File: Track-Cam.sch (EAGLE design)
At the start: 40 parts, among them IC1 STM32F042K6T, IC2 BD6211F, IC3 BD6211F, Q1 8MHz, X1 RASPI_BOARD_B+#_HC

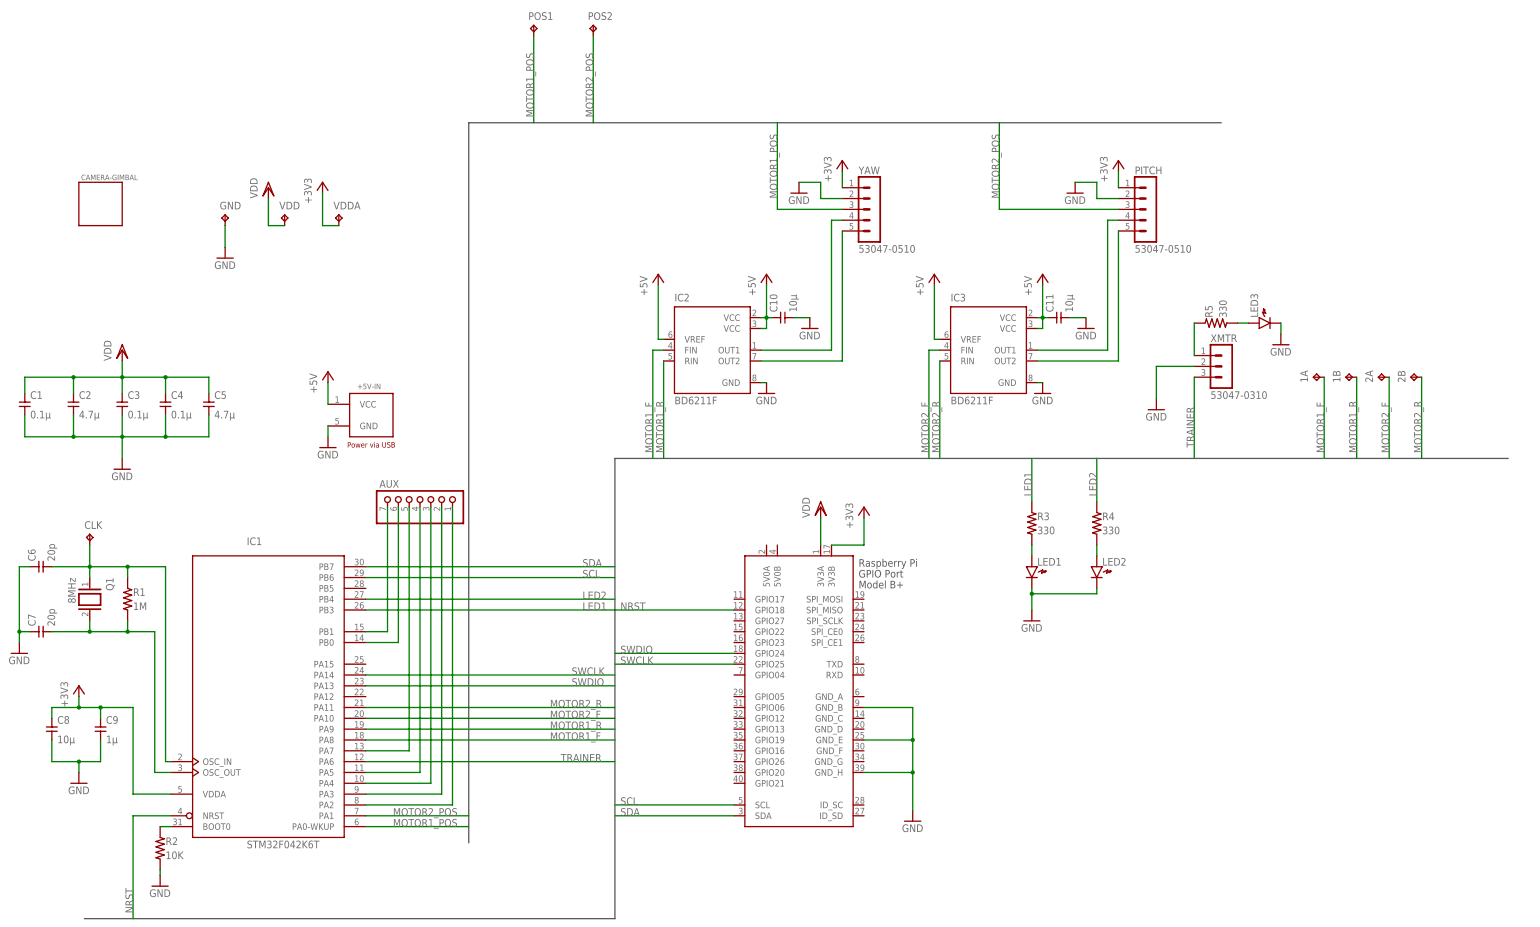
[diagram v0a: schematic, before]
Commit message: enlarge pads
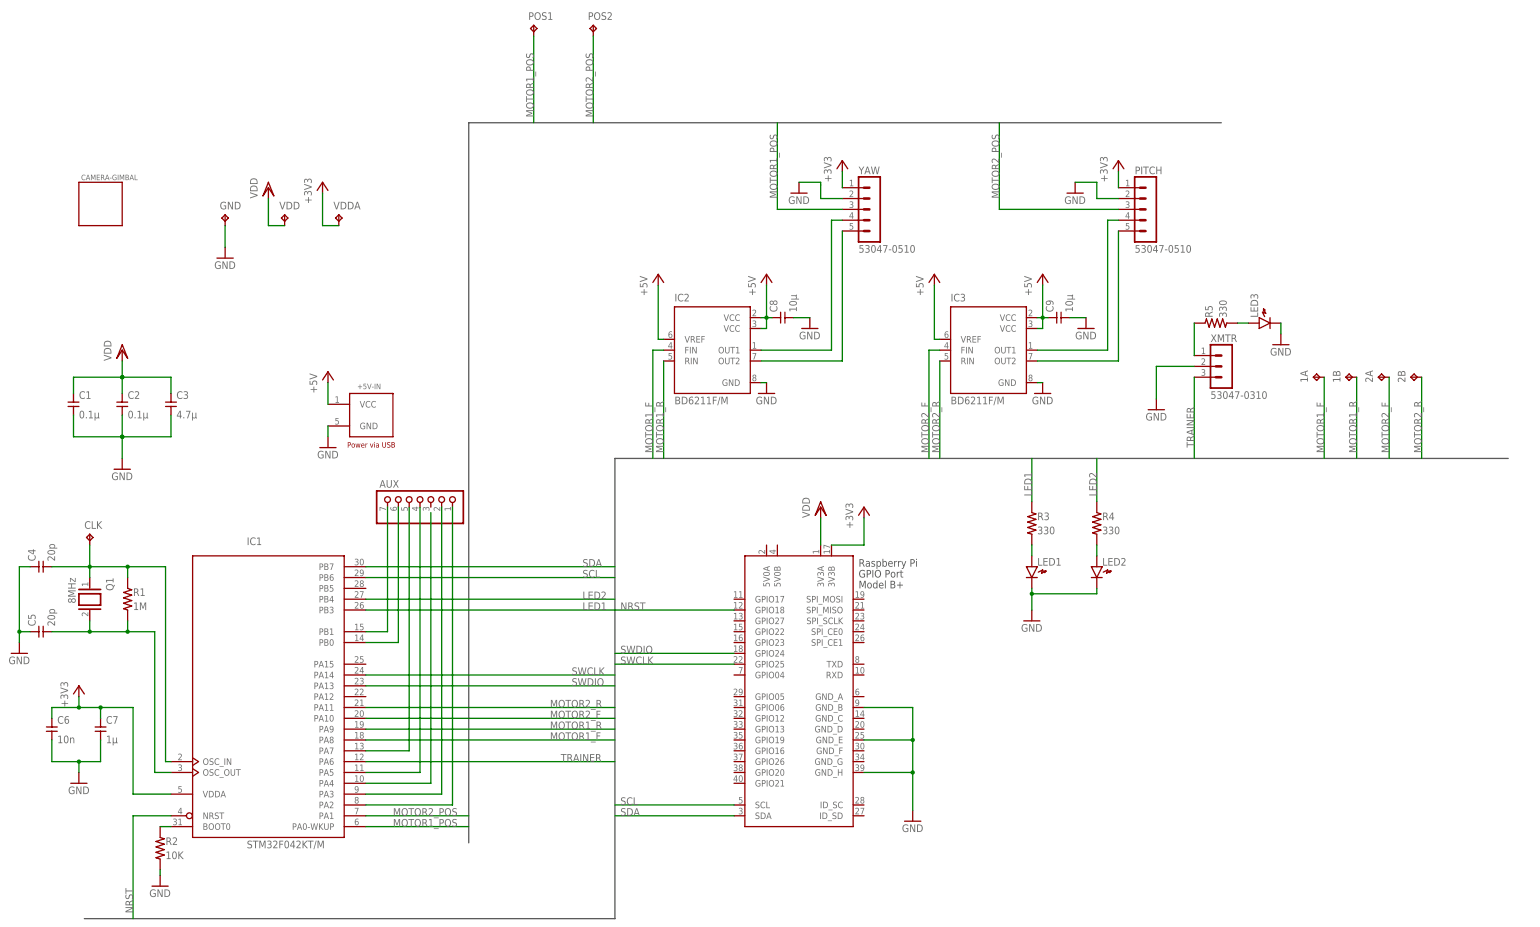
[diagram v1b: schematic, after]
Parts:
- removed C10, C11: 10μ, gen-discrete:CAPACITOR2012
- C2: value 4.7μ -> 0.1μ
- C3: value 0.1μ -> 4.7μ
- C4: value 0.1μ -> 20p
- C5: value 4.7μ -> 20p
- C6: value 20p -> 10n
- C7: value 20p -> 1μ
- C9: value 1μ -> 10μ
- IC1: value STM32F042K6T -> STM32F042KT/M; device stm32:STM32F042K6T -> stm32:STM32F042KT/M
- IC2, IC3: value BD6211F -> BD6211F/M; device rohm-modified:BD6211F -> rohm-modified:BD6211F/M
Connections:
- net PA2 renamed N$1
- net PA3 renamed N$2
- net PA5 renamed N$4
- net PA7 renamed N$5
- net PB0 renamed N$6
- net PB1 renamed N$7
- removed net PA4: AUX.3, IC1MCU.PA4
- new net N$3: IC1MCU.PA4
- net +3V3: now also C6.1, C7.1; no longer C8.1, C9.1
- net +5V: now also C8.1, C9.1; no longer C10.1, C11.1
- net GND: now also C4.1, C5.1, C6.2, C7.2; no longer C10.2, C11.2, C4.2, C5.2, C6.1, C7.1
- net OSC_IN: now also C4.2; no longer C6.2
- net OSC_OUT: now also C5.2; no longer C7.2
- net VDD: no longer C4.1, C5.1
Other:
- moved on the sheet: C1, C2, C3, C4, C5, C6, C7, C8, C9

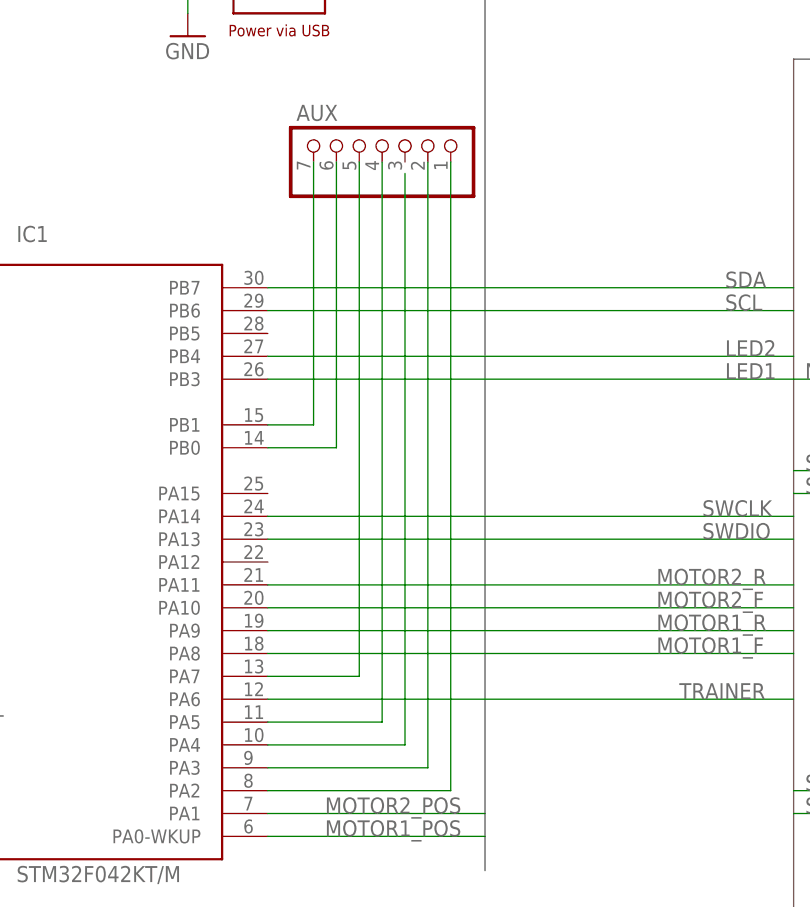
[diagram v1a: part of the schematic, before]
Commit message: fix issue of unconnected path
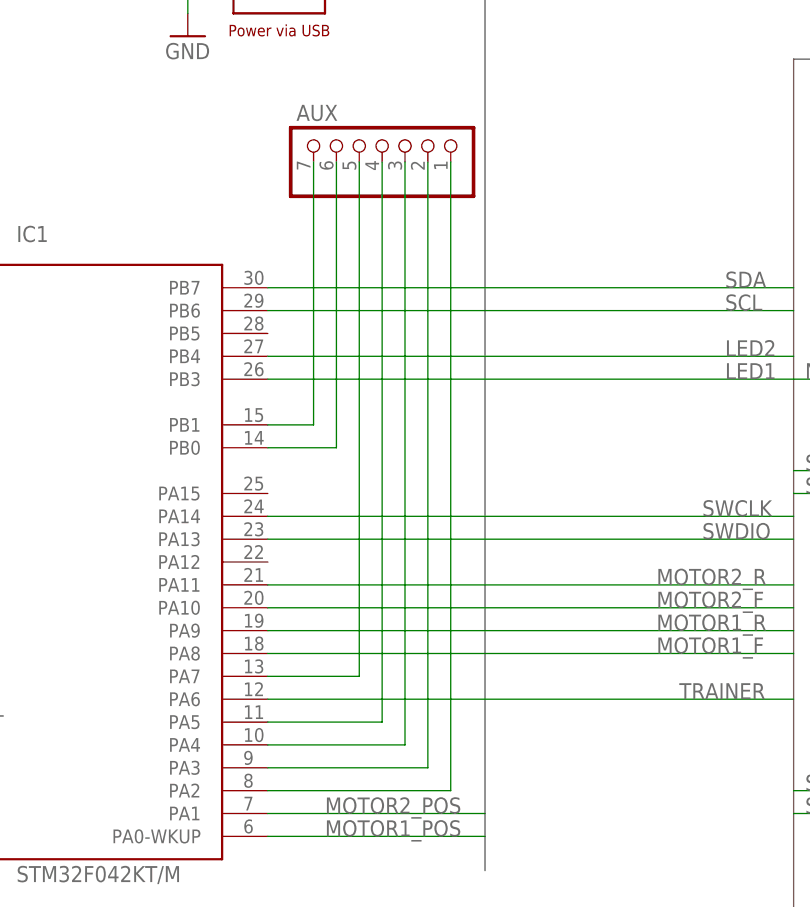
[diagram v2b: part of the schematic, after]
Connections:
- net N$3: now also AUX.3
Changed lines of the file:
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@@
-</segment>
-</net>
-<net name="N$3" class="0">
-<segment>
-<pinref part="IC1" gate="MCU" pin="PA4"/>
-<wire x1="149.86" y1="48.26" x2="165.1" y2="48.26" width="0.1524" layer="91"/>
-<wire x1="165.1" y1="48.26" x2="165.1" y2="111.76" width="0.1524" layer="91"/>
 </segment>
 </net>
@@
 </segment>
 </net>
+<net name="N$3" class="0">
+<segment>
+<pinref part="IC1" gate="MCU" pin="PA4"/>
+<pinref part="AUX" gate="A" pin="3"/>
+<wire x1="149.86" y1="48.26" x2="165.1" y2="48.26" width="0.1524" layer="91"/>
+<wire x1="165.1" y1="48.26" x2="165.1" y2="113.03" width="0.1524" layer="91"/>
+</segment>
+</net>

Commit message: add polygon net
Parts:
- +5V-IN: value MRUSB-2B-D14NI-S306 -> MRUSB-2B-D14NI-S306/M; device connector:MRUSB-2B-D14NI-S306 -> connector:MRUSB-2B-D14NI-S306/M
- renumbered Q1 to XT1
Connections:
- net N$1 renamed PA2
- net N$2 renamed PA3
- net N$3 renamed PA4
- net N$4 renamed PA5
- net N$5 renamed PA7
- net N$6 renamed PB0
- net N$7 renamed PB1
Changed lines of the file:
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@@
 <part name="C6" library="gen-discrete" deviceset="CAPACITOR" device="2012" value="10n"/>
 <part name="C7" library="gen-discrete" deviceset="CAPACITOR" device="2012" value="1μ"/>
-<part name="Q1" library="gen-discrete" deviceset="XTAL/S" device="" value="8MHz"/>
+<part name="XT1" library="gen-discrete" deviceset="XTAL/S" device="" value="8MHz"/>
 <part name="R1" library="gen-discrete" deviceset="RESISTOR-US" device="1608" value="1M"/>
 <part name="R2" library="generic" deviceset="RESISTOR-US" device="1608" value="10K"/>
@@
 <part name="+3V4" library="supply1" deviceset="+3V3" device=""/>
 <part name="GND12" library="supply1" deviceset="GND" device=""/>
-<part name="+5V-IN" library="connector" deviceset="MRUSB-2B-D14NI-S306" device=""/>
+<part name="+5V-IN" library="connector" deviceset="MRUSB-2B-D14NI-S306" device="/M" value="MRUSB-2B-D14NI-S306/M"/>
 <part name="P+5" library="supply1" deviceset="+5V" device=""/>
 <part name="GND13" library="supply1" deviceset="GND" device=""/>
@@
 <instance part="C6" gate="G$1" x="76.2" y="60.96"/>
 <instance part="C7" gate="G$1" x="87.63" y="60.96"/>
-<instance part="Q1" gate="G$1" x="85.09" y="91.44" rot="R270"/>
+<instance part="XT1" gate="G$1" x="85.09" y="91.44" rot="R270"/>
 <instance part="R1" gate="G$1" x="93.98" y="91.44"/>
 <instance part="R2" gate="G$1" x="101.6" y="33.02"/>
@@
 <wire x1="93.98" y1="96.52" x2="93.98" y2="99.06" width="0.1524" layer="91"/>
 <junction x="93.98" y="99.06"/>
-<pinref part="Q1" gate="G$1" pin="1"/>
+<pinref part="XT1" gate="G$1" pin="1"/>
 <wire x1="85.09" y1="96.52" x2="85.09" y2="99.06" width="0.1524" layer="91"/>
 <junction x="85.09" y="99.06"/>
@@
 <wire x1="93.98" y1="86.36" x2="93.98" y2="83.82" width="0.1524" layer="91"/>
 <wire x1="85.09" y1="83.82" x2="93.98" y2="83.82" width="0.1524" layer="91"/>
-<pinref part="Q1" gate="G$1" pin="2"/>
+<pinref part="XT1" gate="G$1" pin="2"/>
 <wire x1="85.09" y1="86.36" x2="85.09" y2="83.82" width="0.1524" layer="91"/>
 <junction x="85.09" y="83.82"/>
@@
 </segment>
 </net>
-<net name="N$1" class="0">
+<net name="PA2" class="0">
 <segment>
 <pinref part="IC1" gate="MCU" pin="PA2"/>
@@
 </segment>
 </net>
-<net name="N$2" class="0">
+<net name="PA3" class="0">
 <segment>
 <pinref part="IC1" gate="MCU" pin="PA3"/>
@@
 </segment>
 </net>
-<net name="N$4" class="0">
+<net name="PA5" class="0">
 <segment>
 <pinref part="IC1" gate="MCU" pin="PA5"/>
@@
 </segment>
 </net>
-<net name="N$5" class="0">
+<net name="PA7" class="0">
 <segment>
 <pinref part="IC1" gate="MCU" pin="PA7"/>
@@
 </segment>
 </net>
-<net name="N$6" class="0">
+<net name="PB0" class="0">
 <segment>
 <pinref part="IC1" gate="MCU" pin="PB0"/>
@@
 </segment>
 </net>
-<net name="N$7" class="0">
+<net name="PB1" class="0">
 <segment>
 <pinref part="IC1" gate="MCU" pin="PB1"/>
@@
 </segment>
 </net>
-<net name="N$3" class="0">
+<net name="PA4" class="0">
 <segment>
 <pinref part="IC1" gate="MCU" pin="PA4"/>
